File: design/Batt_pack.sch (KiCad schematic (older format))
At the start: 7 parts

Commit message: Some small fix in BQ and TODO
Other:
- note added: "Mess bellow. Batt_ball circuit are sharing every pin expect last and first\nSo becase they are sharing pin they are sharing a Rin so only\nlast should have it.(IN every block)."
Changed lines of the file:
@@
 $Descr A4 11693 8268
 encoding utf-8
-Sheet 37 68
+Sheet 5 68
 Title "Battery Pack"
 Date ""
@@
 U 1 1 55BCE59F
 P 6200 1300
+AR Path="/55BB8FBC/3A5B5476/55BCE59F" Ref="D?"  Part="1"
+AR Path="/3A58CB36/55BCE59F" Ref="D?"  Part="1"
 F 0 "D?" H 6200 1400 40  0000 C CNN
 F 1 "DIODE" H 6200 1200 40  0000 C CNN
@@
 U 1 1 3A50FF92
 P 6550 4400
+AR Path="/55BB8FBC/3A5B5476/3A50FF92" Ref="R"  Part="1"
+AR Path="/3A58CB36/3A50FF92" Ref="R"  Part="1"
 F 0 "R" V 6630 4400 40  0000 C CNN
 F 1 "Rf 1M" V 6557 4401 40  0000 C CNN
@@
 U 1 1 3A513D90
 P 6450 4150
+AR Path="/55BB8FBC/3A5B5476/3A513D90" Ref="Cc5"  Part="1"
+AR Path="/3A58CB36/3A513D90" Ref="Cc5"  Part="1"
 F 0 "Cc5" H 6450 4250 40  0000 L CNN
 F 1 "C" H 6456 4065 40  0000 L CNN
@@
 U 1 1 3A5210D8
 P 6500 6100
+AR Path="/55BB8FBC/3A5B5476/3A5210D8" Ref="R?"  Part="1"
+AR Path="/3A58CB36/3A5210D8" Ref="R?"  Part="1"
 F 0 "R?" V 6580 6100 40  0000 C CNN
 F 1 "Rf 1M" V 6507 6101 40  0000 C CNN
@@
 U 1 1 3A5210DE
 P 6400 5850
+AR Path="/55BB8FBC/3A5B5476/3A5210DE" Ref="Cc?"  Part="1"
+AR Path="/3A58CB36/3A5210DE" Ref="Cc?"  Part="1"
 F 0 "Cc?" H 6400 5950 40  0000 L CNN
 F 1 "C" H 6406 5765 40  0000 L CNN
@@
 U 1 1 3A53561F
 P 6550 2700
+AR Path="/55BB8FBC/3A5B5476/3A53561F" Ref="R?"  Part="1"
+AR Path="/3A58CB36/3A53561F" Ref="R?"  Part="1"
 F 0 "R?" V 6630 2700 40  0000 C CNN
 F 1 "Rf 1M" V 6557 2701 40  0000 C CNN
@@
 U 1 1 3A535626
 P 6450 2450
+AR Path="/55BB8FBC/3A5B5476/3A535626" Ref="Cc?"  Part="1"
+AR Path="/3A58CB36/3A535626" Ref="Cc?"  Part="1"
 F 0 "Cc?" H 6450 2550 40  0000 L CNN
 F 1 "C" H 6456 2365 40  0000 L CNN
@@
 Text HLabel 6550 1300 2    60   Input ~ 0
 BATT
+Text Notes 4150 950  0    60   ~ 0
+Mess bellow. Batt_ball circuit are sharing every pin expect last and first\nSo becase they are sharing pin they are sharing a Rin so only\nlast should have it.(IN every block).
 $EndSCHEMATC

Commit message: Renew pdf set some vaules add links and more comments
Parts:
- R, R? (x2): value Rf 1M -> Rf 1K
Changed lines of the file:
@@
 $Descr A4 11693 8268
 encoding utf-8
-Sheet 5 68
+Sheet 5 101
 Title "Battery Pack"
 Date ""
@@
 AR Path="/3A58CB36/3A50FF92" Ref="R"  Part="1"
 F 0 "R" V 6630 4400 40  0000 C CNN
-F 1 "Rf 1M" V 6557 4401 40  0000 C CNN
+F 1 "Rf 1K" V 6557 4401 40  0000 C CNN
 F 2 "" V 6480 4400 30  0000 C CNN
 F 3 "" H 6550 4400 30  0000 C CNN
@@
 AR Path="/3A58CB36/3A5210D8" Ref="R?"  Part="1"
 F 0 "R?" V 6580 6100 40  0000 C CNN
-F 1 "Rf 1M" V 6507 6101 40  0000 C CNN
+F 1 "Rf 1K" V 6507 6101 40  0000 C CNN
 F 2 "" V 6430 6100 30  0000 C CNN
 F 3 "" H 6500 6100 30  0000 C CNN
@@
 AR Path="/3A58CB36/3A53561F" Ref="R?"  Part="1"
 F 0 "R?" V 6630 2700 40  0000 C CNN
-F 1 "Rf 1M" V 6557 2701 40  0000 C CNN
+F 1 "Rf 1K" V 6557 2701 40  0000 C CNN
 F 2 "" V 6480 2700 30  0000 C CNN
 F 3 "" H 6550 2700 30  0000 C CNN

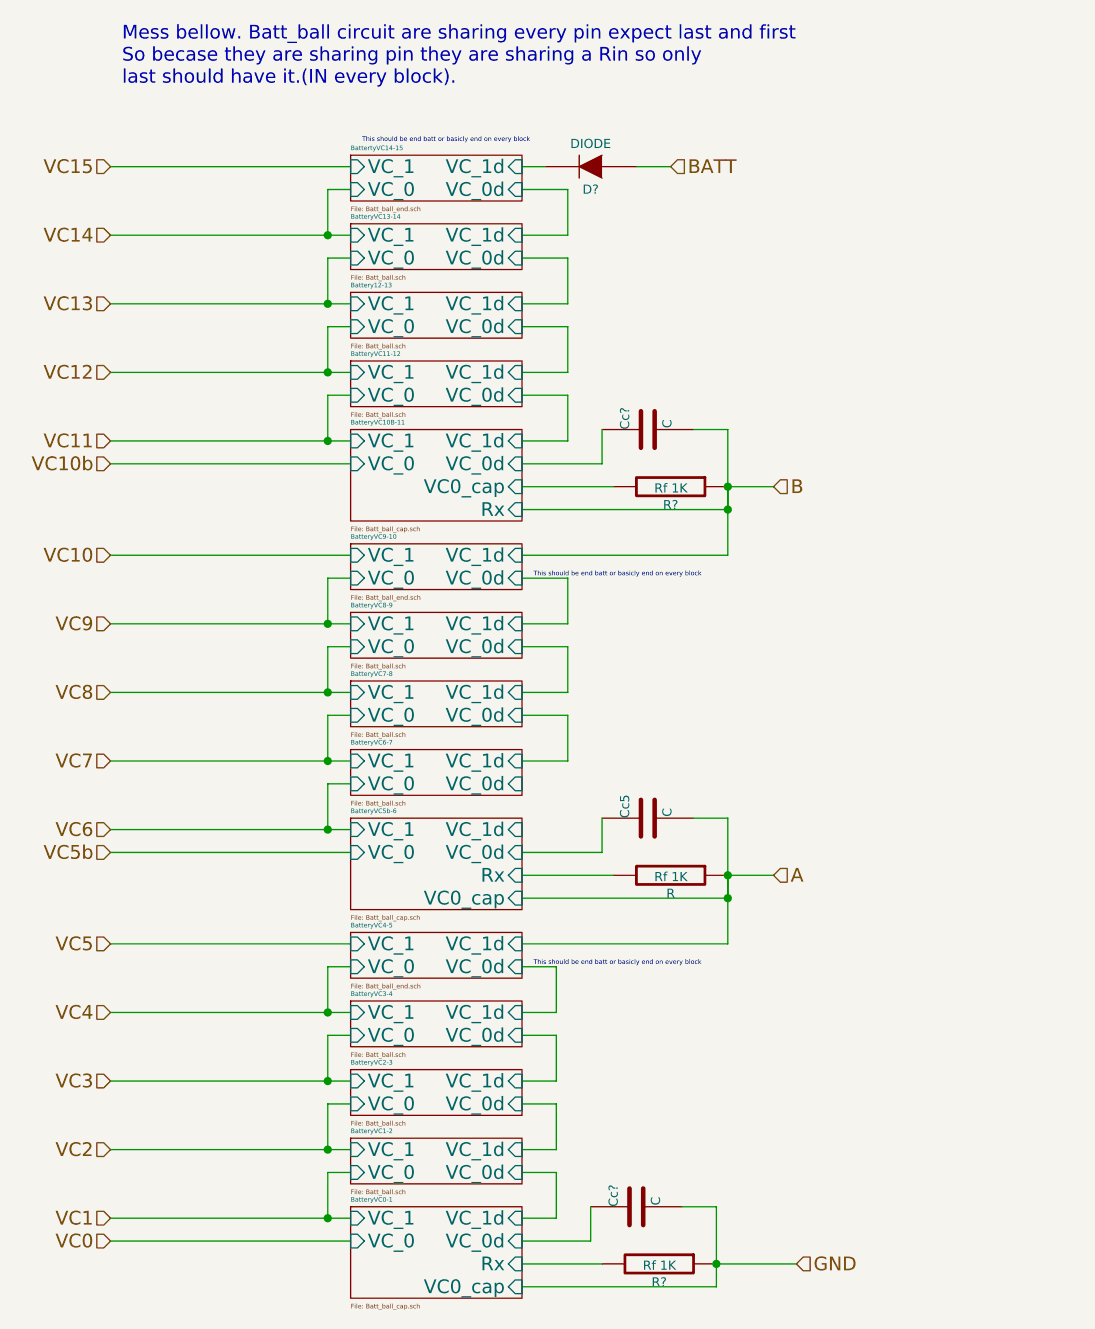
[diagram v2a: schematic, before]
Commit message: Fix some schematic update pdf
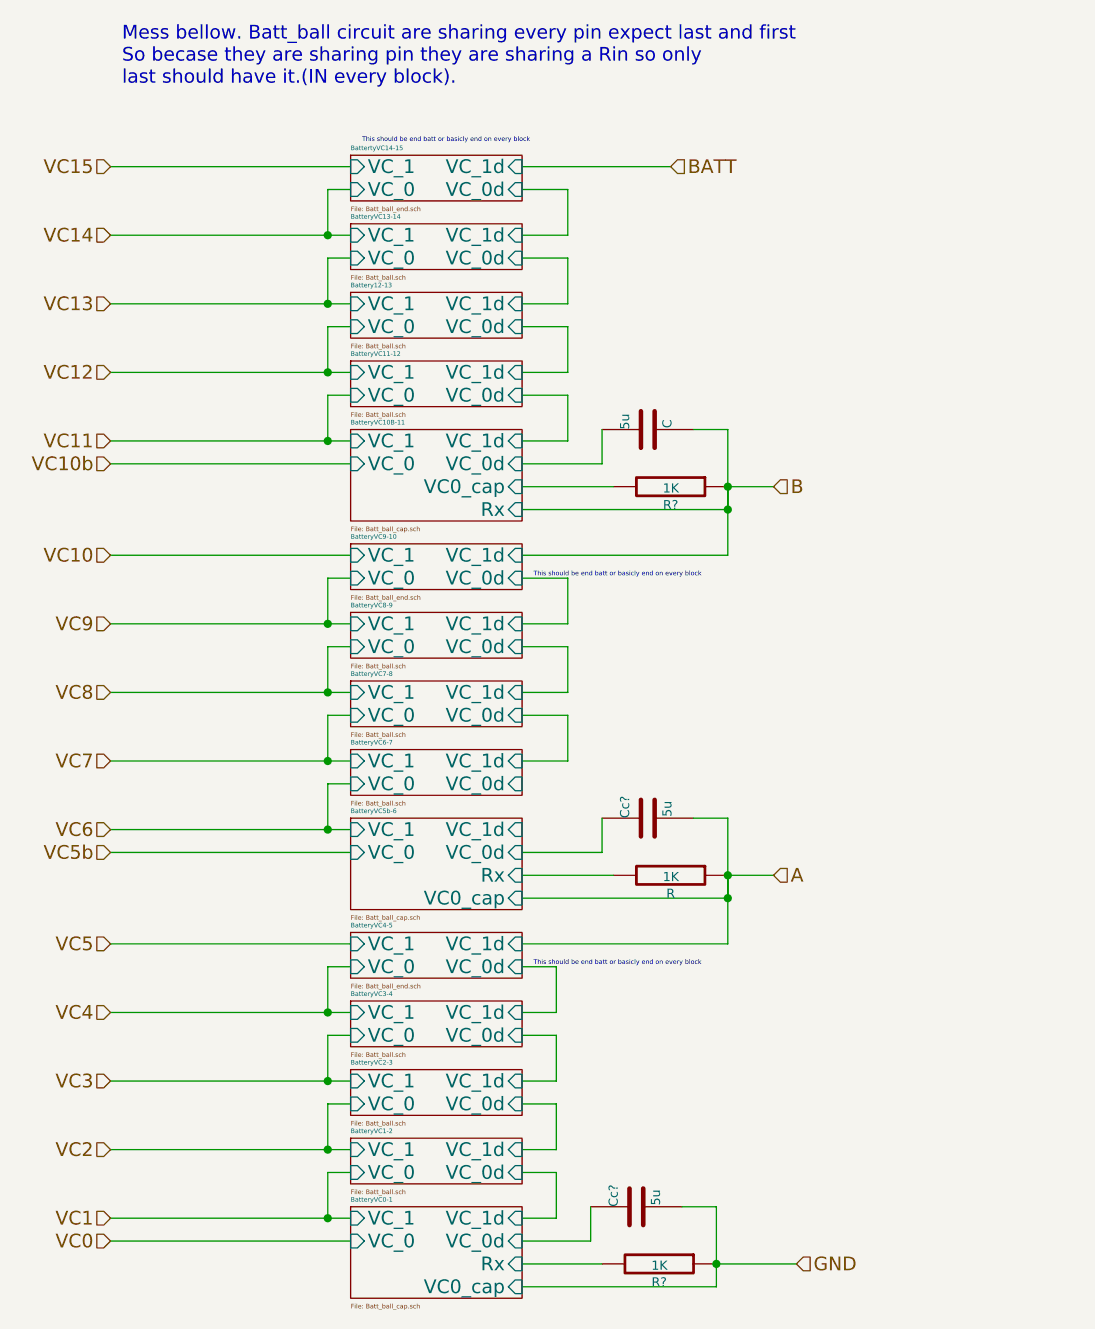
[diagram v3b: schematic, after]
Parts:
- removed D?: DIODE, symbol DIODE
- Cc5, Cc?: value C -> 5u
- R, R? (x2): value Rf 1K -> 1K
- gave numbers to parts that had none: 1
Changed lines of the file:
@@
 Comment4 ""
 $EndDescr
-$Comp
-L DIODE D?
-U 1 1 55BCE59F
-P 6200 1300
-AR Path="/55BB8FBC/3A5B5476/55BCE59F" Ref="D?"  Part="1"
-AR Path="/3A58CB36/55BCE59F" Ref="D?"  Part="1"
-F 0 "D?" H 6200 1400 40  0000 C CNN
-F 1 "DIODE" H 6200 1200 40  0000 C CNN
-F 2 "" H 6200 1300 60  0000 C CNN
-F 3 "" H 6200 1300 60  0000 C CNN
-	1    6200 1300
-	-1   0    0    1
-$EndComp
 $Sheet
 S 5150 5550 750  200
@@
 AR Path="/55BB8FBC/3A5B5476/3A50FF92" Ref="R"  Part="1"
 AR Path="/3A58CB36/3A50FF92" Ref="R"  Part="1"
+AR Path="/55C14E4B/3A5B5476/3A50FF92" Ref="R"  Part="1"
 F 0 "R" V 6630 4400 40  0000 C CNN
-F 1 "Rf 1K" V 6557 4401 40  0000 C CNN
+F 1 "1K" V 6557 4401 40  0000 C CNN
 F 2 "" V 6480 4400 30  0000 C CNN
 F 3 "" H 6550 4400 30  0000 C CNN
@@
 $EndComp
 $Comp
-L C Cc5
+L C Cc?
 U 1 1 3A513D90
 P 6450 4150
-AR Path="/55BB8FBC/3A5B5476/3A513D90" Ref="Cc5"  Part="1"
+AR Path="/55BB8FBC/3A5B5476/3A513D90" Ref="Cc?"  Part="1"
 AR Path="/3A58CB36/3A513D90" Ref="Cc5"  Part="1"
-F 0 "Cc5" H 6450 4250 40  0000 L CNN
-F 1 "C" H 6456 4065 40  0000 L CNN
+AR Path="/55C14E4B/3A5B5476/3A513D90" Ref="Cc5"  Part="1"
+F 0 "Cc?" H 6450 4250 40  0000 L CNN
+F 1 "5u" H 6456 4065 40  0000 L CNN
 F 2 "" H 6488 4000 30  0000 C CNN
 F 3 "" H 6450 4150 60  0000 C CNN
@@
 AR Path="/55BB8FBC/3A5B5476/3A5210D8" Ref="R?"  Part="1"
 AR Path="/3A58CB36/3A5210D8" Ref="R?"  Part="1"
+AR Path="/55C14E4B/3A5B5476/3A5210D8" Ref="R?"  Part="1"
 F 0 "R?" V 6580 6100 40  0000 C CNN
-F 1 "Rf 1K" V 6507 6101 40  0000 C CNN
+F 1 "1K" V 6507 6101 40  0000 C CNN
 F 2 "" V 6430 6100 30  0000 C CNN
 F 3 "" H 6500 6100 30  0000 C CNN
@@
 AR Path="/55BB8FBC/3A5B5476/3A5210DE" Ref="Cc?"  Part="1"
 AR Path="/3A58CB36/3A5210DE" Ref="Cc?"  Part="1"
+AR Path="/55C14E4B/3A5B5476/3A5210DE" Ref="Cc?"  Part="1"
 F 0 "Cc?" H 6400 5950 40  0000 L CNN
-F 1 "C" H 6406 5765 40  0000 L CNN
+F 1 "5u" H 6406 5765 40  0000 L CNN
 F 2 "" H 6438 5700 30  0000 C CNN
 F 3 "" H 6400 5850 60  0000 C CNN
@@
 AR Path="/55BB8FBC/3A5B5476/3A53561F" Ref="R?"  Part="1"
 AR Path="/3A58CB36/3A53561F" Ref="R?"  Part="1"
+AR Path="/55C14E4B/3A5B5476/3A53561F" Ref="R?"  Part="1"
 F 0 "R?" V 6630 2700 40  0000 C CNN
-F 1 "Rf 1K" V 6557 2701 40  0000 C CNN
+F 1 "1K" V 6557 2701 40  0000 C CNN
 F 2 "" V 6480 2700 30  0000 C CNN
 F 3 "" H 6550 2700 30  0000 C CNN
@@
 $EndComp
 $Comp
-L C Cc?
+L C 5u
 U 1 1 3A535626
 P 6450 2450
-AR Path="/55BB8FBC/3A5B5476/3A535626" Ref="Cc?"  Part="1"
+AR Path="/55BB8FBC/3A5B5476/3A535626" Ref="5u"  Part="1"
 AR Path="/3A58CB36/3A535626" Ref="Cc?"  Part="1"
-F 0 "Cc?" H 6450 2550 40  0000 L CNN
+AR Path="/55C14E4B/3A5B5476/3A535626" Ref="Cc?"  Part="1"
+F 0 "5u" H 6450 2550 40  0000 L CNN
 F 1 "C" H 6456 2365 40  0000 L CNN
 F 2 "" H 6488 2300 30  0000 C CNN
@@
 This should be end batt or basicly end on every block
 Wire Wire Line
-	5900 1300 6000 1300
-Wire Wire Line
-	6400 1300 6550 1300
+	5900 1300 6550 1300
 Wire Wire Line
 	5900 4400 6300 4400
